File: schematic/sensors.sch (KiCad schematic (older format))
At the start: 14 parts

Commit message: prototype footprint and placement test
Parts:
- C7, C8: renamed from C?; footprint (none) -> Capacitor_SMD:C_0805_2012Metric_Pad1.15x1.40mm_HandSolder
- J12, J14: renamed from J?; footprint (none) -> Connector_JST:JST_XH_B3B-XH-AM_1x03_P2.50mm_Vertical
- J13: renamed from J?; footprint (none) -> Connector_JST:JST_XH_B2B-XH-AM_1x02_P2.50mm_Vertical
- J15, J16, J17: renamed from J?; footprint (none) -> Connector_JST:JST_XH_B3B-XH-A_1x03_P2.50mm_Vertical
- R12, R13, R14, R15, R16: renamed from R?; footprint (none) -> Resistor_SMD:R_0805_2012Metric_Pad1.15x1.40mm_HandSolder
- gave numbers to parts that had none: 1

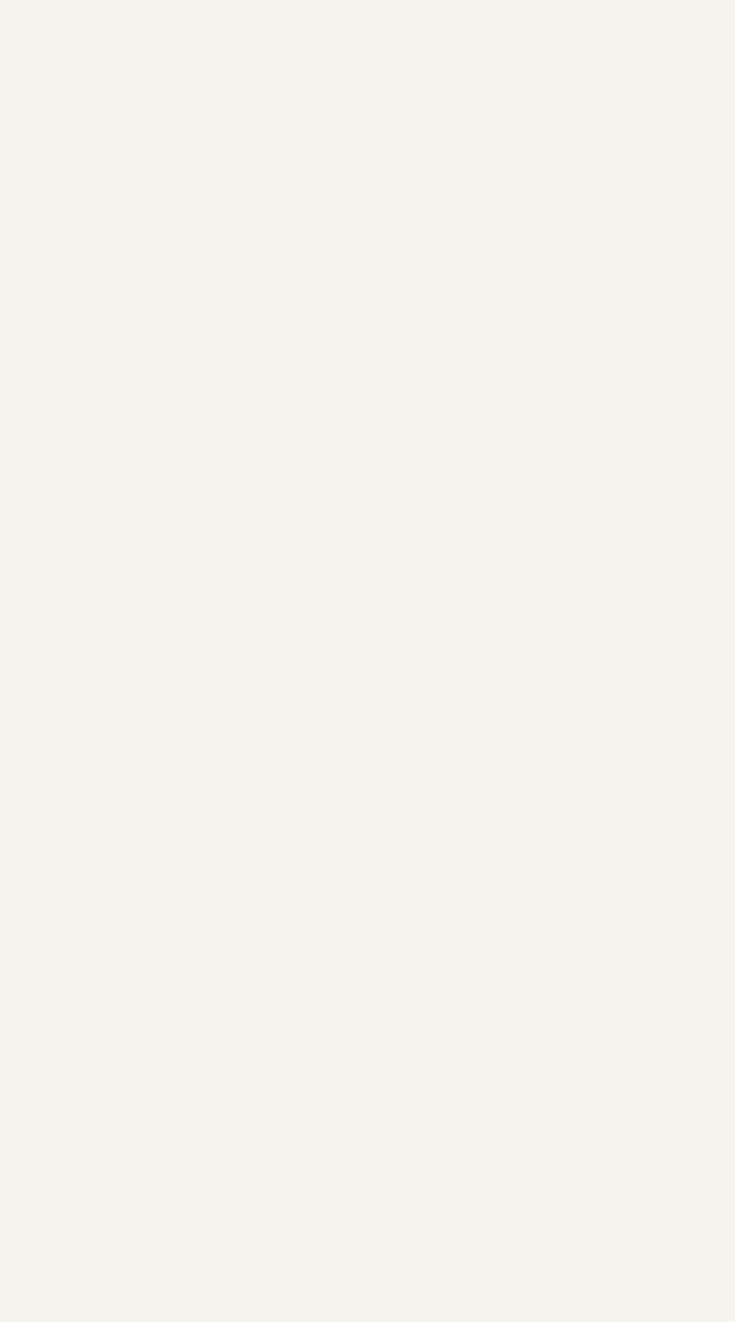
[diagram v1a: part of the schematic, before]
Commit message: added LSM6DSOX and LIS2MDL for IMU
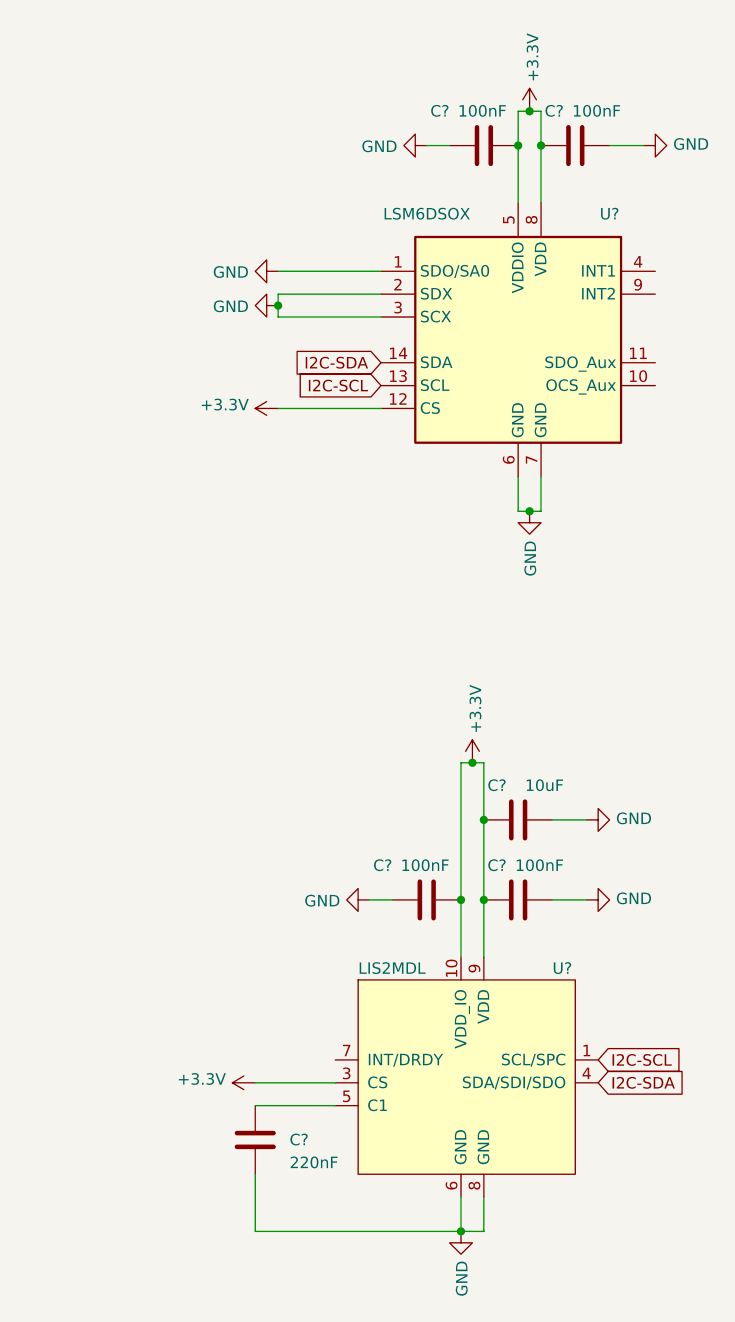
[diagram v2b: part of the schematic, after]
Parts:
- added C? (x4): 100nF, Capacitor_SMD:C_0805_2012Metric_Pad1.15x1.40mm_HandSolder, symbol Device:C
- added C?: 10uF, Capacitor_SMD:C_0805_2012Metric_Pad1.15x1.40mm_HandSolder, symbol Device:C
- added C?: 220nF, Capacitor_SMD:C_0805_2012Metric_Pad1.15x1.40mm_HandSolder, symbol Device:C
- added U?: LIS2MDL, Package_LGA:LGA-12_2x2mm_P0.5mm, symbol Apsu_Library:LIS2MDL
- added U?: LSM6DSOX, Package_LGA:LGA-14_3x2.5mm_P0.5mm_LayoutBorder3x4y, symbol Apsu_Library:LSM6DSOX
- J12, J14: footprint Connector_JST:JST_XH_B3B-XH-AM_1x03_P2.50mm_Vertical -> Connector_JST:JST_XH_B3B-XH-A_1x03_P2.50mm_Vertical
- J13: footprint Connector_JST:JST_XH_B2B-XH-AM_1x02_P2.50mm_Vertical -> Connector_JST:JST_XH_B2B-XH-A_1x02_P2.50mm_Vertical
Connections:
- wire segments 5 -> 40

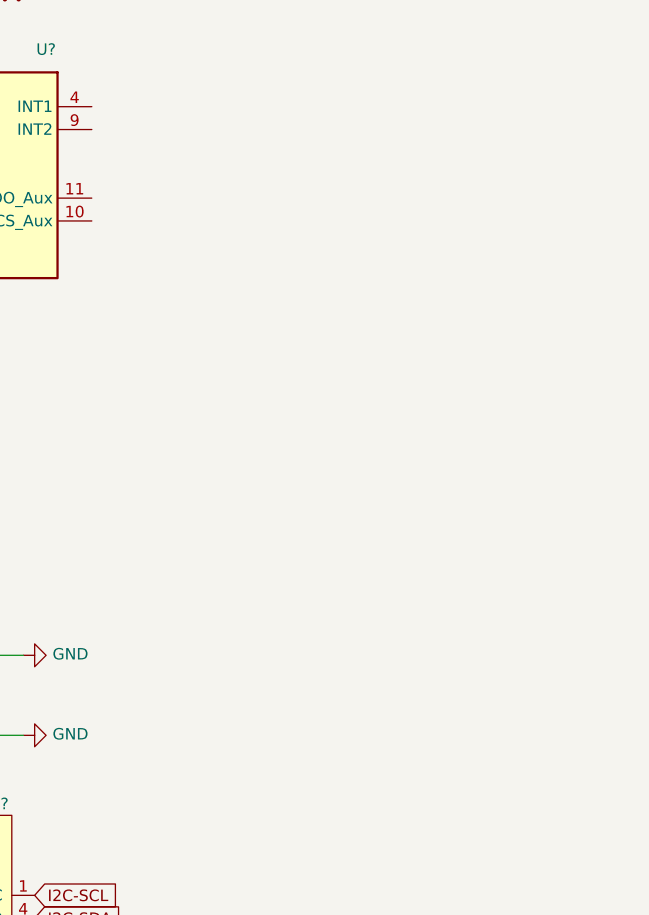
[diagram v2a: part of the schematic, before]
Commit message: added BME280
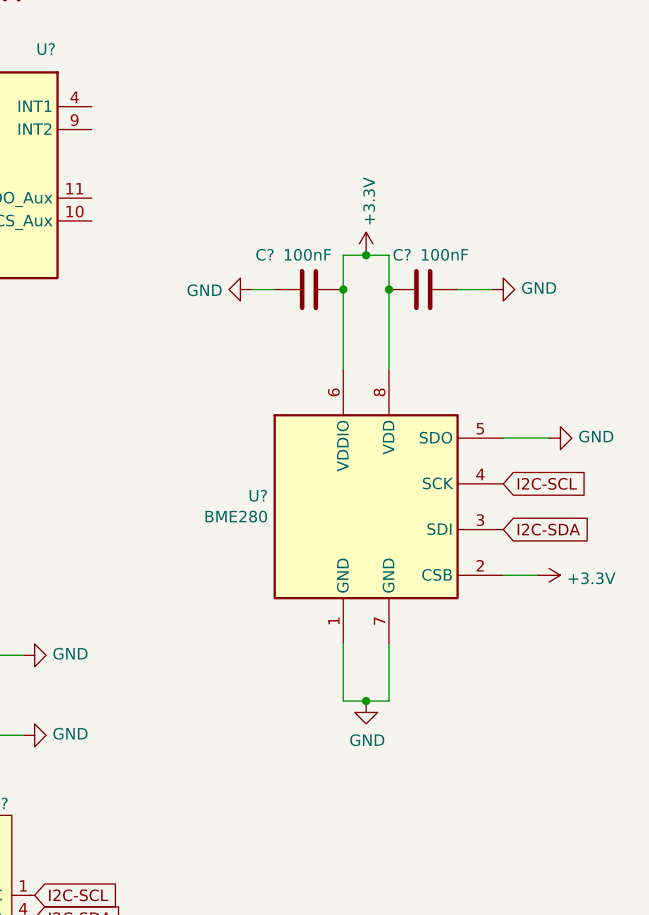
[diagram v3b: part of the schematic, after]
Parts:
- added C? (x2): 100nF, Capacitor_SMD:C_0805_2012Metric_Pad1.15x1.40mm_HandSolder, symbol Device:C
- added U?: BME280, Package_LGA:Bosch_LGA-8_2.5x2.5mm_P0.65mm_ClockwisePinNumbering, symbol Sensor:BME280
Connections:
- wire segments 40 -> 54
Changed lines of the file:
@@
 	1    0    0    -1
 $EndComp
+$Comp
+L power:GND #PWR?
+U 1 1 5EE0F747
+P 9600 4250
+F 0 "#PWR?" H 9600 4000 50  0001 C CNN
+F 1 "GND" H 9605 4077 50  0000 C CNN
+F 2 "" H 9600 4250 50  0001 C CNN
+F 3 "" H 9600 4250 50  0001 C CNN
+	1    9600 4250
+	1    0    0    -1
+$EndComp
+Wire Wire Line
+	9500 4000 9500 4250
+Wire Wire Line
+	9500 4250 9600 4250
+Wire Wire Line
+	9700 4000 9700 4250
+Wire Wire Line
+	9700 4250 9600 4250
+Connection ~ 9600 4250
+$Comp
+L power:+3.3V #PWR?
+U 1 1 5EE11E57
+P 10350 3700
+F 0 "#PWR?" H 10350 3550 50  0001 C CNN
+F 1 "+3.3V" V 10365 3828 50  0000 L CNN
+F 2 "" H 10350 3700 50  0001 C CNN
+F 3 "" H 10350 3700 50  0001 C CNN
+	1    10350 3700
+	0    1    1    0
+$EndComp
+Wire Wire Line
+	10200 3700 10350 3700
+Text GLabel 10200 3500 2    50   Input ~ 0
+I2C-SDA
+Text GLabel 10200 3300 2    50   Input ~ 0
+I2C-SCL
+$Comp
+L power:GND #PWR?
+U 1 1 5EE1306F
+P 10400 3100
+F 0 "#PWR?" H 10400 2850 50  0001 C CNN
+F 1 "GND" V 10405 2972 50  0000 R CNN
+F 2 "" H 10400 3100 50  0001 C CNN
+F 3 "" H 10400 3100 50  0001 C CNN
+	1    10400 3100
+	0    -1   -1   0
+$EndComp
+Wire Wire Line
+	10200 3100 10400 3100
+$Comp
+L power:+3.3V #PWR?
+U 1 1 5EE18751
+P 9600 2300
+AR Path="/5EE18751" Ref="#PWR?"  Part="1"
+AR Path="/5EF89400/5EE18751" Ref="#PWR?"  Part="1"
+F 0 "#PWR?" H 9600 2150 50  0001 C CNN
+F 1 "+3.3V" V 9615 2428 50  0000 L CNN
+F 2 "" H 9600 2300 50  0001 C CNN
+F 3 "" H 9600 2300 50  0001 C CNN
+	1    9600 2300
+	1    0    0    -1
+$EndComp
+$Comp
+L Device:C C?
+U 1 1 5EE1875D
+P 9850 2450
+AR Path="/5EE1875D" Ref="C?"  Part="1"
+AR Path="/5EF89400/5EE1875D" Ref="C?"  Part="1"
+F 0 "C?" V 10000 2500 50  0000 L CNN
+F 1 "100nF" V 10000 2250 50  0000 L CNN
+F 2 "Capacitor_SMD:C_0805_2012Metric_Pad1.15x1.40mm_HandSolder" H 9888 2300 50  0001 C CNN
+F 3 "~" H 9850 2450 50  0001 C CNN
+	1    9850 2450
+	0    -1   -1   0
+$EndComp
+$Comp
+L power:GND #PWR?
+U 1 1 5EE18769
+P 10150 2450
+AR Path="/5EE18769" Ref="#PWR?"  Part="1"
+AR Path="/5EF89400/5EE18769" Ref="#PWR?"  Part="1"
+F 0 "#PWR?" H 10150 2200 50  0001 C CNN
+F 1 "GND" V 10155 2322 50  0000 R CNN
+F 2 "" H 10150 2450 50  0001 C CNN
+F 3 "" H 10150 2450 50  0001 C CNN
+	1    10150 2450
+	0    -1   -1   0
+$EndComp
+Connection ~ 9600 2300
+Wire Wire Line
+	10000 2450 10150 2450
+Wire Wire Line
+	9200 2450 9100 2450
+$Comp
+L power:GND #PWR?
+U 1 1 5EE18763
+P 9100 2450
+AR Path="/5EE18763" Ref="#PWR?"  Part="1"
+AR Path="/5EF89400/5EE18763" Ref="#PWR?"  Part="1"
+F 0 "#PWR?" H 9100 2200 50  0001 C CNN
+F 1 "GND" V 9105 2322 50  0000 R CNN
+F 2 "" H 9100 2450 50  0001 C CNN
+F 3 "" H 9100 2450 50  0001 C CNN
+	1    9100 2450
+	0    1    1    0
+$EndComp
+$Comp
+L Device:C C?
+U 1 1 5EE18757
+P 9350 2450
+AR Path="/5EE18757" Ref="C?"  Part="1"
+AR Path="/5EF89400/5EE18757" Ref="C?"  Part="1"
+F 0 "C?" V 9500 2600 50  0000 L CNN
+F 1 "100nF" V 9500 2350 50  0000 L CNN
+F 2 "Capacitor_SMD:C_0805_2012Metric_Pad1.15x1.40mm_HandSolder" H 9388 2300 50  0001 C CNN
+F 3 "~" H 9350 2450 50  0001 C CNN
+	1    9350 2450
+	0    -1   -1   0
+$EndComp
+$Comp
+L Sensor:BME280 U?
+U 1 1 5EE0D3B6
+P 9600 3400
+F 0 "U?" H 9171 3446 50  0000 R CNN
+F 1 "BME280" H 9171 3355 50  0000 R CNN
+F 2 "Package_LGA:Bosch_LGA-8_2.5x2.5mm_P0.65mm_ClockwisePinNumbering" H 11100 2950 50  0001 C CNN
+F 3 "https://ae-bst.resource.bosch.com/media/_tech/media/datasheets/BST-BME280-DS002.pdf" H 9600 3200 50  0001 C CNN
+	1    9600 3400
+	1    0    0    -1
+$EndComp
+Wire Wire Line
+	9700 2300 9700 2450
+Wire Wire Line
+	9600 2300 9700 2300
+Wire Wire Line
+	9700 2450 9700 2800
+Connection ~ 9700 2450
+Wire Wire Line
+	9500 2300 9500 2450
+Wire Wire Line
+	9500 2300 9600 2300
+Wire Wire Line
+	9500 2450 9500 2800
+Connection ~ 9500 2450
 $EndSCHEMATC

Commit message: new pcb design
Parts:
- gave numbers to parts that had none: 11
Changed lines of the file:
@@
 P 6750 1800
 AR Path="/5EDF7B63" Ref="#PWR?"  Part="1"
-AR Path="/5EF89400/5EDF7B63" Ref="#PWR?"  Part="1"
-F 0 "#PWR?" H 6750 1550 50  0001 C CNN
+AR Path="/5EF89400/5EDF7B63" Ref="#PWR061"  Part="1"
+F 0 "#PWR061" H 6750 1550 50  0001 C CNN
 F 1 "GND" V 6755 1672 50  0000 R CNN
 F 2 "" H 6750 1800 50  0001 C CNN
@@
 P 7850 950
 AR Path="/5EDFAB5E" Ref="#PWR?"  Part="1"
-AR Path="/5EF89400/5EDFAB5E" Ref="#PWR?"  Part="1"
-F 0 "#PWR?" H 7850 800 50  0001 C CNN
+AR Path="/5EF89400/5EDFAB5E" Ref="#PWR067"  Part="1"
+F 0 "#PWR067" H 7850 800 50  0001 C CNN
 F 1 "+3.3V" V 7865 1078 50  0000 L CNN
 F 2 "" H 7850 950 50  0001 C CNN
@@
 P 7650 1100
 AR Path="/5EDFB4FF" Ref="C?"  Part="1"
-AR Path="/5EF89400/5EDFB4FF" Ref="C?"  Part="1"
-F 0 "C?" V 7800 1250 50  0000 L CNN
+AR Path="/5EF89400/5EDFB4FF" Ref="C13"  Part="1"
+F 0 "C13" V 7800 1250 50  0000 L CNN
 F 1 "100nF" V 7800 1000 50  0000 L CNN
 F 2 "Capacitor_SMD:C_0805_2012Metric_Pad1.15x1.40mm_HandSolder" H 7688 950 50  0001 C CNN
@@
 P 8050 1100
 AR Path="/5EDFBC6F" Ref="C?"  Part="1"
-AR Path="/5EF89400/5EDFBC6F" Ref="C?"  Part="1"
-F 0 "C?" V 8200 1150 50  0000 L CNN
+AR Path="/5EF89400/5EDFBC6F" Ref="C16"  Part="1"
+F 0 "C16" V 8200 1150 50  0000 L CNN
 F 1 "100nF" V 8200 900 50  0000 L CNN
 F 2 "Capacitor_SMD:C_0805_2012Metric_Pad1.15x1.40mm_HandSolder" H 8088 950 50  0001 C CNN
@@
 P 7400 1100
 AR Path="/5EDFC9EE" Ref="#PWR?"  Part="1"
-AR Path="/5EF89400/5EDFC9EE" Ref="#PWR?"  Part="1"
-F 0 "#PWR?" H 7400 850 50  0001 C CNN
+AR Path="/5EF89400/5EDFC9EE" Ref="#PWR064"  Part="1"
+F 0 "#PWR064" H 7400 850 50  0001 C CNN
 F 1 "GND" V 7405 972 50  0000 R CNN
 F 2 "" H 7400 1100 50  0001 C CNN
@@
 P 8350 1100
 AR Path="/5EDFCF30" Ref="#PWR?"  Part="1"
-AR Path="/5EF89400/5EDFCF30" Ref="#PWR?"  Part="1"
-F 0 "#PWR?" H 8350 850 50  0001 C CNN
+AR Path="/5EF89400/5EDFCF30" Ref="#PWR071"  Part="1"
+F 0 "#PWR071" H 8350 850 50  0001 C CNN
 F 1 "GND" V 8355 972 50  0000 R CNN
 F 2 "" H 8350 1100 50  0001 C CNN
@@
 P 7850 2700
 AR Path="/5EDFE18D" Ref="#PWR?"  Part="1"
-AR Path="/5EF89400/5EDFE18D" Ref="#PWR?"  Part="1"
-F 0 "#PWR?" H 7850 2450 50  0001 C CNN
+AR Path="/5EF89400/5EDFE18D" Ref="#PWR068"  Part="1"
+F 0 "#PWR068" H 7850 2450 50  0001 C CNN
 F 1 "GND" V 7855 2572 50  0000 R CNN
 F 2 "" H 7850 2700 50  0001 C CNN
@@
 P 6750 2250
 AR Path="/5EE10356" Ref="#PWR?"  Part="1"
-AR Path="/5EF89400/5EE10356" Ref="#PWR?"  Part="1"
-F 0 "#PWR?" H 6750 2100 50  0001 C CNN
+AR Path="/5EF89400/5EE10356" Ref="#PWR062"  Part="1"
+F 0 "#PWR062" H 6750 2100 50  0001 C CNN
 F 1 "+3.3V" V 6765 2378 50  0000 L CNN
 F 2 "" H 6750 2250 50  0001 C CNN
@@
 P 6750 1650
 AR Path="/5EE12FAB" Ref="#PWR?"  Part="1"
-AR Path="/5EF89400/5EE12FAB" Ref="#PWR?"  Part="1"
-F 0 "#PWR?" H 6750 1400 50  0001 C CNN
+AR Path="/5EF89400/5EE12FAB" Ref="#PWR036"  Part="1"
+F 0 "#PWR036" H 6750 1400 50  0001 C CNN
 F 1 "GND" V 6755 1522 50  0000 R CNN
 F 2 "" H 6750 1650 50  0001 C CNN
@@
 	6750 1650 7200 1650
 $Comp
-L Apsu_Library:LIS2MDL U?
+L Apsu_Library:LIS2MDL U6
 U 1 1 5EE414BE
 P 7600 5200
-F 0 "U?" H 7950 5700 50  0000 L CNN
+F 0 "U6" H 7950 5700 50  0000 L CNN
 F 1 "LIS2MDL" H 7100 5700 50  0000 L CNN
 F 2 "Package_LGA:LGA-12_2x2mm_P0.5mm" H 8500 4650 50  0001 C CNN
@@
 P 7600 3800
 AR Path="/5EE49417" Ref="#PWR?"  Part="1"
-AR Path="/5EF89400/5EE49417" Ref="#PWR?"  Part="1"
-F 0 "#PWR?" H 7600 3650 50  0001 C CNN
+AR Path="/5EF89400/5EE49417" Ref="#PWR066"  Part="1"
+F 0 "#PWR066" H 7600 3650 50  0001 C CNN
 F 1 "+3.3V" V 7615 3928 50  0000 L CNN
 F 2 "" H 7600 3800 50  0001 C CNN
@@
 P 7400 4400
 AR Path="/5EE4941D" Ref="C?"  Part="1"
-AR Path="/5EF89400/5EE4941D" Ref="C?"  Part="1"
-F 0 "C?" V 7550 4550 50  0000 L CNN
+AR Path="/5EF89400/5EE4941D" Ref="C12"  Part="1"
+F 0 "C12" V 7550 4550 50  0000 L CNN
 F 1 "100nF" V 7550 4300 50  0000 L CNN
 F 2 "Capacitor_SMD:C_0805_2012Metric_Pad1.15x1.40mm_HandSolder" H 7438 4250 50  0001 C CNN
@@
 P 7800 4400
 AR Path="/5EE49423" Ref="C?"  Part="1"
-AR Path="/5EF89400/5EE49423" Ref="C?"  Part="1"
-F 0 "C?" V 7950 4450 50  0000 L CNN
+AR Path="/5EF89400/5EE49423" Ref="C15"  Part="1"
+F 0 "C15" V 7950 4450 50  0000 L CNN
 F 1 "100nF" V 7950 4200 50  0000 L CNN
 F 2 "Capacitor_SMD:C_0805_2012Metric_Pad1.15x1.40mm_HandSolder" H 7838 4250 50  0001 C CNN
@@
 P 7150 4400
 AR Path="/5EE49429" Ref="#PWR?"  Part="1"
-AR Path="/5EF89400/5EE49429" Ref="#PWR?"  Part="1"
-F 0 "#PWR?" H 7150 4150 50  0001 C CNN
+AR Path="/5EF89400/5EE49429" Ref="#PWR063"  Part="1"
+F 0 "#PWR063" H 7150 4150 50  0001 C CNN
 F 1 "GND" V 7155 4272 50  0000 R CNN
 F 2 "" H 7150 4400 50  0001 C CNN
@@
 P 8100 4400
 AR Path="/5EE4942F" Ref="#PWR?"  Part="1"
-AR Path="/5EF89400/5EE4942F" Ref="#PWR?"  Part="1"
-F 0 "#PWR?" H 8100 4150 50  0001 C CNN
+AR Path="/5EF89400/5EE4942F" Ref="#PWR070"  Part="1"
+F 0 "#PWR070" H 8100 4150 50  0001 C CNN
 F 1 "GND" V 8105 4272 50  0000 R CNN
 F 2 "" H 8100 4400 50  0001 C CNN
@@
 P 7800 4050
 AR Path="/5EE53247" Ref="C?"  Part="1"
-AR Path="/5EF89400/5EE53247" Ref="C?"  Part="1"
-F 0 "C?" V 7950 4100 50  0000 L CNN
+AR Path="/5EF89400/5EE53247" Ref="C14"  Part="1"
+F 0 "C14" V 7950 4100 50  0000 L CNN
 F 1 "10uF" V 7950 3850 50  0000 L CNN
 F 2 "Capacitor_SMD:C_0805_2012Metric_Pad1.15x1.40mm_HandSolder" H 7838 3900 50  0001 C CNN
@@
 P 8100 4050
 AR Path="/5EE538EC" Ref="#PWR?"  Part="1"
-AR Path="/5EF89400/5EE538EC" Ref="#PWR?"  Part="1"
-F 0 "#PWR?" H 8100 3800 50  0001 C CNN
+AR Path="/5EF89400/5EE538EC" Ref="#PWR069"  Part="1"
+F 0 "#PWR069" H 8100 3800 50  0001 C CNN
 F 1 "GND" V 8105 3922 50  0000 R CNN
 F 2 "" H 8100 4050 50  0001 C CNN
@@
 P 6650 5450
 AR Path="/5EE551FD" Ref="C?"  Part="1"
-AR Path="/5EF89400/5EE551FD" Ref="C?"  Part="1"
-F 0 "C?" H 6800 5450 50  0000 L CNN
+AR Path="/5EF89400/5EE551FD" Ref="C11"  Part="1"
+F 0 "C11" H 6800 5450 50  0000 L CNN
 F 1 "220nF" H 6800 5350 50  0000 L CNN
 F 2 "Capacitor_SMD:C_0805_2012Metric_Pad1.15x1.40mm_HandSolder" H 6688 5300 50  0001 C CNN
@@
 P 7550 5850
 AR Path="/5EE5FEA2" Ref="#PWR?"  Part="1"
-AR Path="/5EF89400/5EE5FEA2" Ref="#PWR?"  Part="1"
-F 0 "#PWR?" H 7550 5600 50  0001 C CNN
+AR Path="/5EF89400/5EE5FEA2" Ref="#PWR065"  Part="1"
+F 0 "#PWR065" H 7550 5600 50  0001 C CNN
 F 1 "GND" V 7555 5722 50  0000 R CNN
 F 2 "" H 7550 5850 50  0001 C CNN
@@
 P 6650 5200
 AR Path="/5EE6E503" Ref="#PWR?"  Part="1"
-AR Path="/5EF89400/5EE6E503" Ref="#PWR?"  Part="1"
-F 0 "#PWR?" H 6650 5050 50  0001 C CNN
+AR Path="/5EF89400/5EE6E503" Ref="#PWR035"  Part="1"
+F 0 "#PWR035" H 6650 5050 50  0001 C CNN
 F 1 "+3.3V" V 6665 5328 50  0000 L CNN
 F 2 "" H 6650 5200 50  0001 C CNN
@@
 	7550 5850 7650 5850
 $Comp
-L Apsu_Library:LSM6DSOX U?
+L Apsu_Library:LSM6DSOX U7
 U 1 1 5EE990C5
 P 7800 1950
-F 0 "U?" H 8200 2500 50  0000 C CNN
+F 0 "U7" H 8200 2500 50  0000 C CNN
 F 1 "LSM6DSOX" H 7400 2500 50  0000 C CNN
 F 2 "Package_LGA:LGA-14_3x2.5mm_P0.5mm_LayoutBorder3x4y" H 7400 1250 50  0001 L CNN
@@
 $EndComp
 $Comp
-L power:GND #PWR?
+L power:GND #PWR074
 U 1 1 5EE0F747
 P 9600 4250
-F 0 "#PWR?" H 9600 4000 50  0001 C CNN
+F 0 "#PWR074" H 9600 4000 50  0001 C CNN
 F 1 "GND" H 9605 4077 50  0000 C CNN
 F 2 "" H 9600 4250 50  0001 C CNN
@@
 Connection ~ 9600 4250
 $Comp
-L power:+3.3V #PWR?
+L power:+3.3V #PWR076
 U 1 1 5EE11E57
 P 10350 3700
-F 0 "#PWR?" H 10350 3550 50  0001 C CNN
+F 0 "#PWR076" H 10350 3550 50  0001 C CNN
 F 1 "+3.3V" V 10365 3828 50  0000 L CNN
 F 2 "" H 10350 3700 50  0001 C CNN
@@
 I2C-SCL
 $Comp
-L power:GND #PWR?
+L power:GND #PWR077
 U 1 1 5EE1306F
 P 10400 3100
-F 0 "#PWR?" H 10400 2850 50  0001 C CNN
+F 0 "#PWR077" H 10400 2850 50  0001 C CNN
 F 1 "GND" V 10405 2972 50  0000 R CNN
 F 2 "" H 10400 3100 50  0001 C CNN
@@
 P 9600 2300
 AR Path="/5EE18751" Ref="#PWR?"  Part="1"
-AR Path="/5EF89400/5EE18751" Ref="#PWR?"  Part="1"
-F 0 "#PWR?" H 9600 2150 50  0001 C CNN
+AR Path="/5EF89400/5EE18751" Ref="#PWR073"  Part="1"
+F 0 "#PWR073" H 9600 2150 50  0001 C CNN
 F 1 "+3.3V" V 9615 2428 50  0000 L CNN
 F 2 "" H 9600 2300 50  0001 C CNN
@@
 P 9850 2450
 AR Path="/5EE1875D" Ref="C?"  Part="1"
-AR Path="/5EF89400/5EE1875D" Ref="C?"  Part="1"
-F 0 "C?" V 10000 2500 50  0000 L CNN
+AR Path="/5EF89400/5EE1875D" Ref="C18"  Part="1"
+F 0 "C18" V 10000 2500 50  0000 L CNN
 F 1 "100nF" V 10000 2250 50  0000 L CNN
 F 2 "Capacitor_SMD:C_0805_2012Metric_Pad1.15x1.40mm_HandSolder" H 9888 2300 50  0001 C CNN
@@
 P 10150 2450
 AR Path="/5EE18769" Ref="#PWR?"  Part="1"
-AR Path="/5EF89400/5EE18769" Ref="#PWR?"  Part="1"
-F 0 "#PWR?" H 10150 2200 50  0001 C CNN
+AR Path="/5EF89400/5EE18769" Ref="#PWR075"  Part="1"
+F 0 "#PWR075" H 10150 2200 50  0001 C CNN
 F 1 "GND" V 10155 2322 50  0000 R CNN
 F 2 "" H 10150 2450 50  0001 C CNN
@@
 P 9100 2450
 AR Path="/5EE18763" Ref="#PWR?"  Part="1"
-AR Path="/5EF89400/5EE18763" Ref="#PWR?"  Part="1"
-F 0 "#PWR?" H 9100 2200 50  0001 C CNN
+AR Path="/5EF89400/5EE18763" Ref="#PWR072"  Part="1"
+F 0 "#PWR072" H 9100 2200 50  0001 C CNN
 F 1 "GND" V 9105 2322 50  0000 R CNN
 F 2 "" H 9100 2450 50  0001 C CNN
@@
 P 9350 2450
 AR Path="/5EE18757" Ref="C?"  Part="1"
-AR Path="/5EF89400/5EE18757" Ref="C?"  Part="1"
-F 0 "C?" V 9500 2600 50  0000 L CNN
+AR Path="/5EF89400/5EE18757" Ref="C17"  Part="1"
+F 0 "C17" V 9500 2600 50  0000 L CNN
 F 1 "100nF" V 9500 2350 50  0000 L CNN
 F 2 "Capacitor_SMD:C_0805_2012Metric_Pad1.15x1.40mm_HandSolder" H 9388 2300 50  0001 C CNN
@@
 $EndComp
 $Comp
-L Sensor:BME280 U?
+L Sensor:BME280 U8
 U 1 1 5EE0D3B6
 P 9600 3400
-F 0 "U?" H 9171 3446 50  0000 R CNN
+F 0 "U8" H 9171 3446 50  0000 R CNN
 F 1 "BME280" H 9171 3355 50  0000 R CNN
 F 2 "Package_LGA:Bosch_LGA-8_2.5x2.5mm_P0.65mm_ClockwisePinNumbering" H 11100 2950 50  0001 C CNN

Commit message: boost converter on Apsu board and PCB design
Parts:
- removed U4: MAX11613, Package_SO:MSOP-8_3x3mm_P0.65mm, symbol Analog_ADC:MAX11613
- added C7: 2.2uF, Capacitor_SMD:C_0805_2012Metric_Pad1.15x1.40mm_HandSolder, symbol Device:C
- added C8: 4.7uF, Capacitor_SMD:C_0805_2012Metric_Pad1.15x1.40mm_HandSolder, symbol Device:C
- added L1: 1uH, Inductor_SMD:L_0805_2012Metric_Pad1.15x1.40mm_HandSolder, symbol Device:L
- added U3: ADS1015IDGS, Package_SO:TSSOP-10_3x3mm_P0.5mm, symbol Analog_ADC:ADS1015IDGS
- added U4: FAN4860UC5X, Package_CSP:WLCSP-6_1.4x1.0mm_P0.4mm, symbol Apsu_Library:FAN4860UC5X
- renumbered C12 to C10, C13 to C11, C14 to C12, C15 to C13, C16 to C14, C17 to C15, C18 to C16, C7 to C5, C8 to C6, C11 to C9, J16 to J10, J17 to J11, J12 to J6, J13 to J7, J14 to J8, J15 to J9, U6 to U5, U7 to U6, U8 to U7
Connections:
- wire segments 54 -> 70
